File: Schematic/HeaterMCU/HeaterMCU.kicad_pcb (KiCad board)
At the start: 2 copper layers, 100 x 35 mm, 60 parts, among them J301 Conn_01x06, J302 Heater Control, J303 High voltage warning, J304 Firmware, SW301 RESET, U301 Display_IPS_1.3_SPI, U302 ATMEGA328P-AU, U303 TLP185, U304 INA219AIDCNR, U305 TLP185, U306 TPS54302, Y301 8MHz

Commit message: Swapped IO pins
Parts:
- J301: value Conn_01x06 -> To PSU Board
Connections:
- U302 pad 12: Heater_EN -> unconnected-(U302-Pad12)
- U302 pad 22: Disp_RES -> unconnected-(U302-Pad22)
- U302 pad 23: Disp_DC -> Disp_RES
- U302 pad 24: unconnected-(U302-Pad24) -> Disp_DC
- U302 pad 9: unconnected-(U302-Pad9) -> Heater_EN
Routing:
- net Heater_EN: track 28.9 -> 26.3 mm
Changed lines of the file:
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@@
   (net 50 "unconnected-(U302-Pad25)")
   (net 51 "unconnected-(U302-Pad10)")
-  (net 52 "unconnected-(U302-Pad9)")
-  (net 53 "unconnected-(U302-Pad24)")
+  (net 52 "unconnected-(U302-Pad12)")
+  (net 53 "unconnected-(U302-Pad22)")
   (footprint "Capacitor_SMD:C_0603_1608Metric_Pad1.08x0.95mm_HandSolder" (layer "F.Cu")
     (at 101.975 68.325)
@@
     (fp_line (start -1.6 -1.245) (end 1.6 -1.245) (layer "F.Fab") (width 0.1))
     (fp_line (start -1.6 1.245) (end -1.6 -1.245) (layer "F.Fab") (width 0.1))
-    (pad "1" smd roundrect (at -1.55 0 270) (size 1.3 2.65) (layers "F.Cu" "F.Paste" "F.Mask") (roundrect_rratio 0.192308)
+    (pad "1" smd roundrect (at -1.55 0 270) (size 1.3 2.65) (layers "F.Cu" "F.Paste" "F.Mask") (roundrect_rratio 0.1923076923)
       (net 26 "Net-(D304-Pad1)") (pintype "passive"))
-    (pad "2" smd roundrect (at 1.55 0 270) (size 1.3 2.65) (layers "F.Cu" "F.Paste" "F.Mask") (roundrect_rratio 0.192308)
+    (pad "2" smd roundrect (at 1.55 0 270) (size 1.3 2.65) (layers "F.Cu" "F.Paste" "F.Mask") (roundrect_rratio 0.1923076923)
       (net 32 "Net-(J302-Pad2)") (pintype "passive"))
     (model "${KICAD6_3DMODEL_DIR}/Resistor_SMD.3dshapes/R_1210_3225Metric.wrl"
@@
     (fp_line (start 1.6 -1.245) (end 1.6 1.245) (layer "F.Fab") (width 0.1))
     (fp_line (start -1.6 -1.245) (end 1.6 -1.245) (layer "F.Fab") (width 0.1))
-    (pad "1" smd roundrect (at -1.55 0 270) (size 1.3 2.65) (layers "F.Cu" "F.Paste" "F.Mask") (roundrect_rratio 0.192308)
+    (pad "1" smd roundrect (at -1.55 0 270) (size 1.3 2.65) (layers "F.Cu" "F.Paste" "F.Mask") (roundrect_rratio 0.1923076923)
       (net 30 "Net-(D304-Pad2)") (pintype "passive"))
-    (pad "2" smd roundrect (at 1.55 0 270) (size 1.3 2.65) (layers "F.Cu" "F.Paste" "F.Mask") (roundrect_rratio 0.192308)
+    (pad "2" smd roundrect (at 1.55 0 270) (size 1.3 2.65) (layers "F.Cu" "F.Paste" "F.Mask") (roundrect_rratio 0.1923076923)
       (net 32 "Net-(J302-Pad2)") (pintype "passive"))
     (model "${KICAD6_3DMODEL_DIR}/Resistor_SMD.3dshapes/R_1210_3225Metric.wrl"
@@
       (net 42 "Net-(C305-Pad1)") (pinfunction "XTAL2") (pintype "bidirectional"))
     (pad "9" smd rect locked (at -2.8 -4.2 180) (size 0.55 1.5) (layers "B.Cu" "B.Paste" "B.Mask")
-      (net 52 "unconnected-(U302-Pad9)") (pinfunction "D5(PWM)") (pintype "bidirectional"))
+      (net 19 "Heater_EN") (pinfunction "D5(PWM)") (pintype "bidirectional"))
     (pad "10" smd rect locked (at -2 -4.2 180) (size 0.55 1.5) (layers "B.Cu" "B.Paste" "B.Mask")
-      (net 51 "unconnected-(U302-Pad10)") (pinfunction "D6(PWM)") (pintype "bidirectional"))
+      (net 51 "unconnected-(U302-Pad10)") (pinfunction "D6(PWM)") (pintype "bidirectional+no_connect"))
     (pad "11" smd rect locked (at -1.2 -4.2 180) (size 0.55 1.5) (layers "B.Cu" "B.Paste" "B.Mask")
       (net 8 "RLY_CTRL") (pinfunction "D7") (pintype "bidirectional"))
     (pad "12" smd rect locked (at -0.4 -4.2 180) (size 0.55 1.5) (layers "B.Cu" "B.Paste" "B.Mask")
-      (net 19 "Heater_EN") (pinfunction "D8") (pintype "bidirectional"))
+      (net 52 "unconnected-(U302-Pad12)") (pinfunction "D8") (pintype "bidirectional+no_connect"))
     (pad "13" smd rect locked (at 0.4 -4.2 180) (size 0.55 1.5) (layers "B.Cu" "B.Paste" "B.Mask")
       (net 11 "LED_Heater_ON") (pinfunction "D9(PWM)") (pintype "bidirectional"))
@@
       (net 1 "GNDPWR") (pinfunction "GND") (pintype "power_in"))
     (pad "22" smd rect locked (at 4.2 1.2 180) (size 1.5 0.55) (layers "B.Cu" "B.Paste" "B.Mask")
-      (net 16 "Disp_RES") (pinfunction "A7") (pintype "input"))
+      (net 53 "unconnected-(U302-Pad22)") (pinfunction "A7") (pintype "input+no_connect"))
     (pad "23" smd rect locked (at 4.2 2 180) (size 1.5 0.55) (layers "B.Cu" "B.Paste" "B.Mask")
-      (net 15 "Disp_DC") (pinfunction "A0") (pintype "bidirectional"))
+      (net 16 "Disp_RES") (pinfunction "A0") (pintype "bidirectional"))
     (pad "24" smd rect locked (at 4.2 2.8 180) (size 1.5 0.55) (layers "B.Cu" "B.Paste" "B.Mask")
-      (net 53 "unconnected-(U302-Pad24)") (pinfunction "A1") (pintype "bidirectional"))
+      (net 15 "Disp_DC") (pinfunction "A1") (pintype "bidirectional"))
     (pad "25" smd rect locked (at 2.8 4.2 180) (size 0.55 1.5) (layers "B.Cu" "B.Paste" "B.Mask")
-      (net 50 "unconnected-(U302-Pad25)") (pinfunction "A2") (pintype "bidirectional"))
+      (net 50 "unconnected-(U302-Pad25)") (pinfunction "A2") (pintype "bidirectional+no_connect"))
     (pad "26" smd rect locked (at 2 4.2 180) (size 0.55 1.5) (layers "B.Cu" "B.Paste" "B.Mask")
       (net 27 "unconnected-(U302-Pad26)") (pinfunction "A3") (pintype "bidirectional+no_connect"))
@@
       (effects (font (size 0.8 0.8) (thickness 0.1)) (justify mirror))
     )
-    (fp_text value "Conn_01x06" (at 0 -15.47) (layer "B.Fab")
+    (fp_text value "To PSU Board" (at 0 -15.47) (layer "B.Fab")
       (effects (font (size 1 1) (thickness 0.15)) (justify mirror))
     )
@@
   (segment (start 98 63.795) (end 99.202081 63.795) (width 0.5) (layer "F.Cu") (net 14))
   (segment (start 102.8375 67.430419) (end 102.8375 68.325) (width 0.5) (layer "F.Cu") (net 14))
-  (segment (start 59.305 58.9) (end 57.7625 57.3575) (width 0.25) (layer "B.Cu") (net 15))
-  (segment (start 65.9 58.9) (end 59.305 58.9) (width 0.25) (layer "B.Cu") (net 15))
-  (segment (start 57.96 59.7) (end 57.7625 59.8975) (width 0.25) (layer "B.Cu") (net 16))
-  (segment (start 65.9 59.7) (end 57.96 59.7) (width 0.25) (layer "B.Cu") (net 16))
+  (segment (start 65.1575 57.3575) (end 65.9 58.1) (width 0.25) (layer "B.Cu") (net 15))
+  (segment (start 57.7625 57.3575) (end 65.1575 57.3575) (width 0.25) (layer "B.Cu") (net 15))
+  (segment (start 58.76 58.9) (end 57.7625 59.8975) (width 0.25) (layer "B.Cu") (net 16))
+  (segment (start 65.9 58.9) (end 58.76 58.9) (width 0.25) (layer "B.Cu") (net 16))
   (segment (start 66.35 62.05) (end 58.15 62.05) (width 0.25) (layer "F.Cu") (net 17))
   (segment (start 58.15 62.05) (end 57.7625 62.4375) (width 0.25) (layer "F.Cu") (net 17))
@@
   (segment (start 59.22 63.52) (end 65.72 63.52) (width 0.25) (layer "B.Cu") (net 18))
   (segment (start 57.7625 64.9775) (end 59.22 63.52) (width 0.25) (layer "B.Cu") (net 18))
-  (segment (start 70.975 66.575) (end 71.075 66.675) (width 0.25) (layer "F.Cu") (net 19))
+  (segment (start 73.725 66.675) (end 97.66 66.675) (width 0.25) (layer "F.Cu") (net 19))
   (segment (start 97.66 66.675) (end 98 66.335) (width 0.25) (layer "F.Cu") (net 19))
-  (segment (start 71.075 66.675) (end 97.66 66.675) (width 0.25) (layer "F.Cu") (net 19))
-  (via (at 70.975 66.575) (size 0.8) (drill 0.4) (layers "F.Cu" "B.Cu") (net 19))
-  (segment (start 70.5 66.1) (end 70.5 65.1) (width 0.25) (layer "B.Cu") (net 19))
-  (segment (start 70.975 66.575) (end 70.5 66.1) (width 0.25) (layer "B.Cu") (net 19))
+  (via (at 73.725 66.675) (size 0.8) (drill 0.4) (layers "F.Cu" "B.Cu") (net 19))
+  (segment (start 72.9 65.1) (end 72.9 65.85) (width 0.25) (layer "B.Cu") (net 19))
+  (segment (start 72.9 65.85) (end 73.725 66.675) (width 0.25) (layer "B.Cu") (net 19))
   (segment (start 83 57.975) (end 83.4 58.375) (width 0.25) (layer "F.Cu") (net 20))
   (segment (start 68.925 57.975) (end 83 57.975) (width 0.25) (layer "F.Cu") (net 20))

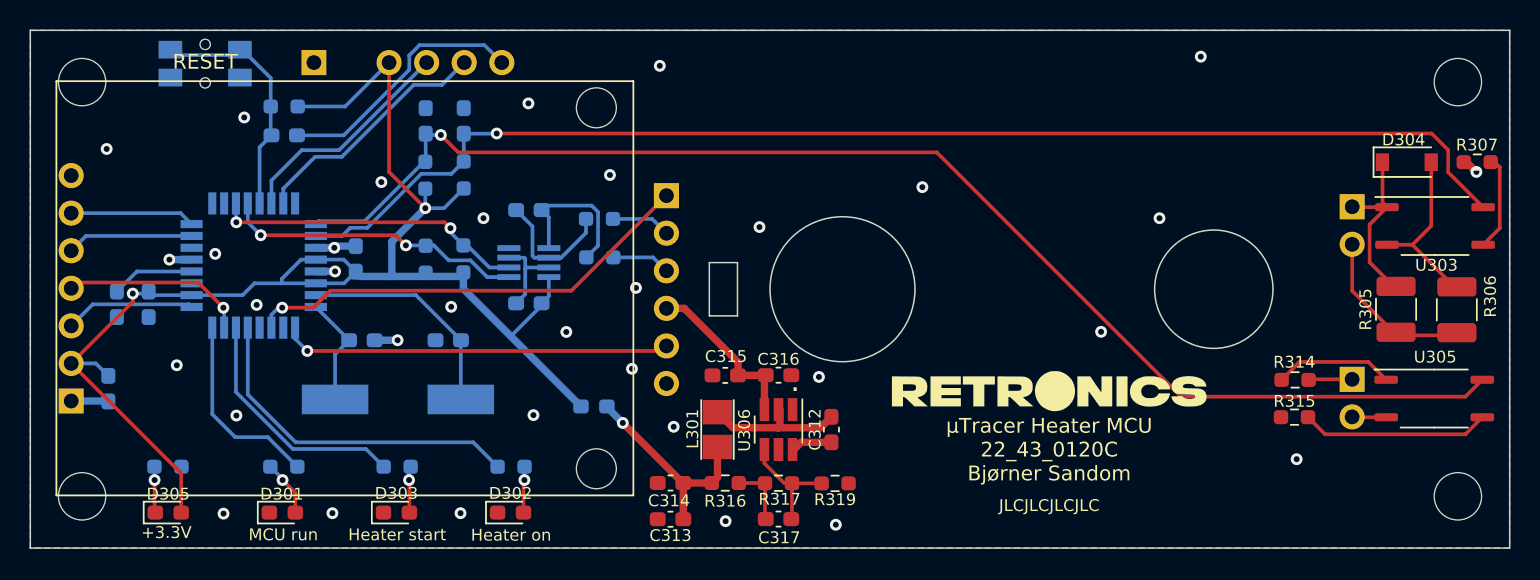
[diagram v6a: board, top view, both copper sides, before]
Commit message: Added PWM controlled MOSFET output for soft start
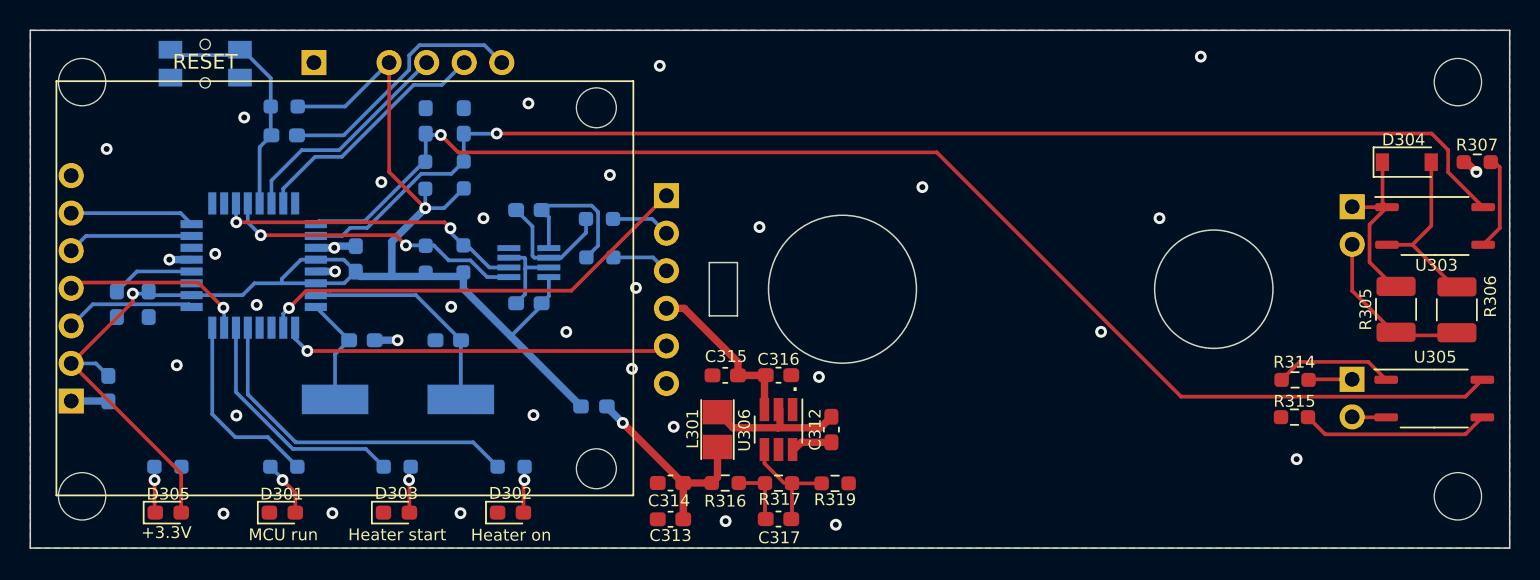
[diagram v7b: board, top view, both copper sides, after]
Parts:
- G***: moved to B.Cu
- moved G*** 21.2 mm to (123.0, 48.1), turned to 180 degrees
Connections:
- J301 pad 1: RLY_CTRL -> Heater_PWM
- U302 pad 10: unconnected-(U302-Pad10) -> Heater_PWM
- U302 pad 11: RLY_CTRL -> unconnected-(U302-Pad11)
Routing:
- net RLY_CTRL: track 30.9 -> 0.00 mm, vias 1 -> 0
- net Heater_PWM: track 0.00 -> 30.2 mm, vias 0 -> 1
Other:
- outline, holes or cut-outs redrawn
